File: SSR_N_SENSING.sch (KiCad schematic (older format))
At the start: 19 parts, among them J1 CONN_01X01, J2 CONN_01X01, J3 CONN_01X01, J4 CONN_01X01, Q1 BC850, U3 ACS722

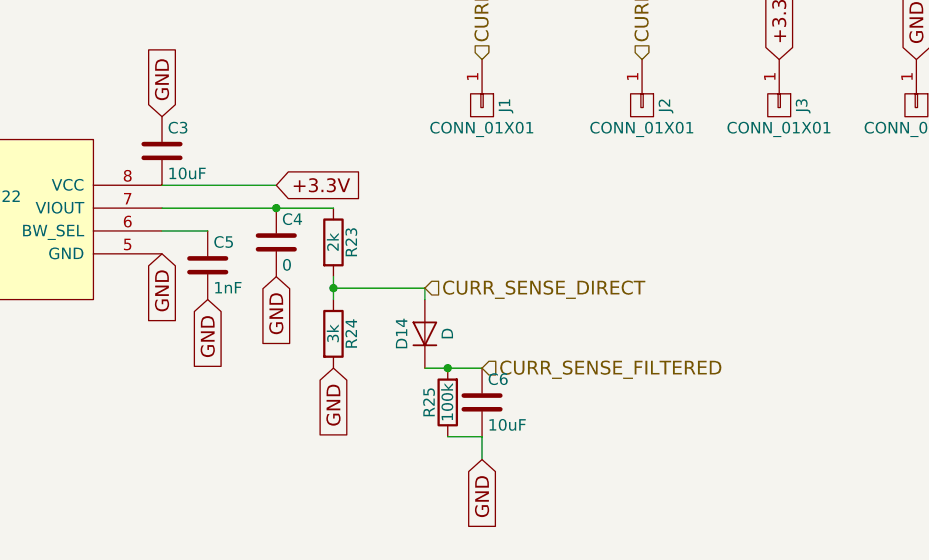
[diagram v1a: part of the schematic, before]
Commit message: I have redirected the output of the acs722 current sensing module directly to the ad converter. In theory this should increase the scale of the current sensing.
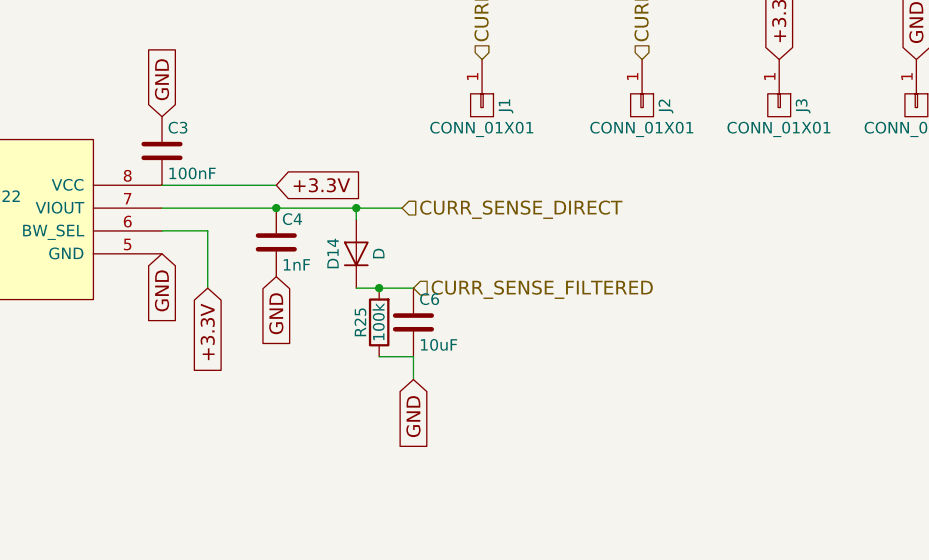
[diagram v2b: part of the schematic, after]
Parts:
- removed C5: 1nF, Capacitors_SMD:C_1206_HandSoldering, symbol C
- removed R23: 2k, Resistors_SMD:R_1206_HandSoldering, symbol R
- removed R24: 3k, Resistors_SMD:R_1206_HandSoldering, symbol R
- C3: value 10uF -> 100nF
- C4: value 0 -> 1nF; Comment This is NOT Necessary -> (none)
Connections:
- net +3.3V: now also U3.6 (BW_SEL)
- net CURR_SENSE_DIRECT: now also C4.1, U3.7 (VIOUT)
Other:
- moved on the sheet: C6, D14, R25
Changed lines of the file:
@@
 P 4950 4100
 F 0 "C3" H 4975 4200 50  0000 L CNN
-F 1 "10uF" H 4975 4000 50  0000 L CNN
+F 1 "100nF" H 4975 4000 50  0000 L CNN
 F 2 "Capacitors_SMD:C_1206_HandSoldering" H 4988 3950 30  0001 C CNN
-F 3 "http://hu.farnell.com/vishay/vj1206y106kxxtw1bc/cap-mlcc-x7r-10uf-25v-1206/dp/2407348" H 4950 4100 60  0001 C CNN
+F 3 "" H 4950 4100 60  0001 C CNN
 	1    4950 4100
 	1    0    0    -1
@@
 P 5450 4500
 F 0 "C4" H 5475 4600 50  0000 L CNN
-F 1 "0" H 5475 4400 50  0000 L CNN
+F 1 "1nF" H 5475 4400 50  0000 L CNN
 F 2 "Capacitors_SMD:C_1206_HandSoldering" H 5488 4350 30  0001 C CNN
 F 3 "" H 5450 4500 60  0000 C CNN
-F 4 "This is NOT Necessary" H 5450 4500 60  0001 C CNN "Comment"
 	1    5450 4500
 	1    0    0    -1
@@
 L D D14
 U 1 1 56251898
-P 6100 4900
-F 0 "D14" H 6100 5000 50  0000 C CNN
-F 1 "D" H 6100 4800 50  0000 C CNN
-F 2 "Diodes_SMD:D_SOD-123" H 6100 4900 60  0001 C CNN
-F 3 "http://hu.farnell.com/taiwan-semiconductor/b0540w/diode-rectif-40v-0-5a-sod123/dp/1863143" H 6100 4900 60  0001 C CNN
-	1    6100 4900
+P 5800 4550
+F 0 "D14" H 5800 4650 50  0000 C CNN
+F 1 "D" H 5800 4450 50  0000 C CNN
+F 2 "Diodes_SMD:D_SOD-123" H 5800 4550 60  0001 C CNN
+F 3 "http://hu.farnell.com/taiwan-semiconductor/b0540w/diode-rectif-40v-0-5a-sod123/dp/1863143" H 5800 4550 60  0001 C CNN
+	1    5800 4550
 	0    -1   -1   0
 $EndComp
@@
 L R R25
 U 1 1 5625189E
-P 6200 5200
-F 0 "R25" V 6280 5200 50  0000 C CNN
-F 1 "100k" V 6200 5200 50  0000 C CNN
-F 2 "Resistors_SMD:R_1206_HandSoldering" V 6130 5200 30  0001 C CNN
-F 3 "http://hu.farnell.com/vishay/crcw1206100kfkea/res-thick-film-100k-1-0-25w-1206/dp/1469975" H 6200 5200 30  0001 C CNN
-	1    6200 5200
+P 5900 4850
+F 0 "R25" V 5980 4850 50  0000 C CNN
+F 1 "100k" V 5900 4850 50  0000 C CNN
+F 2 "Resistors_SMD:R_1206_HandSoldering" V 5830 4850 30  0001 C CNN
+F 3 "http://hu.farnell.com/vishay/crcw1206100kfkea/res-thick-film-100k-1-0-25w-1206/dp/1469975" H 5900 4850 30  0001 C CNN
+	1    5900 4850
 	-1   0    0    1
 $EndComp
@@
 L C C6
 U 1 1 562518A4
-P 6350 5200
-F 0 "C6" H 6375 5300 50  0000 L CNN
-F 1 "10uF" H 6375 5100 50  0000 L CNN
-F 2 "Capacitors_SMD:C_1206_HandSoldering" H 6388 5050 30  0001 C CNN
-F 3 "" H 6350 5200 60  0000 C CNN
-	1    6350 5200
+P 6050 4850
+F 0 "C6" H 6075 4950 50  0000 L CNN
+F 1 "10uF" H 6075 4750 50  0000 L CNN
+F 2 "Capacitors_SMD:C_1206_HandSoldering" H 6088 4700 30  0001 C CNN
+F 3 "" H 6050 4850 60  0000 C CNN
+	1    6050 4850
 	1    0    0    -1
 $EndComp
-Text HLabel 6350 5050 2    60   Input ~ 0
+Text HLabel 6050 4700 2    60   Input ~ 0
 CURR_SENSE_FILTERED
-$Comp
-L C C5
-U 1 1 56251AFD
-P 5150 4600
-F 0 "C5" H 5175 4700 50  0000 L CNN
-F 1 "1nF" H 5175 4500 50  0000 L CNN
-F 2 "Capacitors_SMD:C_1206_HandSoldering" H 5188 4450 30  0001 C CNN
-F 3 "http://hu.farnell.com/vishay/vj1206y102kxeac/cap-mlcc-x7r-1000pf-500v-1206/dp/2407307" H 5150 4600 60  0001 C CNN
-	1    5150 4600
-	1    0    0    -1
-$EndComp
-Text HLabel 6100 4700 2    60   Input ~ 0
+Text HLabel 6000 4350 2    60   Input ~ 0
 CURR_SENSE_DIRECT
-$Comp
-L R R23
-U 1 1 56255AB8
-P 5700 4500
-F 0 "R23" V 5780 4500 50  0000 C CNN
-F 1 "2k" V 5700 4500 50  0000 C CNN
-F 2 "Resistors_SMD:R_1206_HandSoldering" V 5630 4500 30  0001 C CNN
-F 3 "" H 5700 4500 30  0000 C CNN
-	1    5700 4500
-	1    0    0    -1
-$EndComp
-$Comp
-L R R24
-U 1 1 56255B3D
-P 5700 4900
-F 0 "R24" V 5780 4900 50  0000 C CNN
-F 1 "3k" V 5700 4900 50  0000 C CNN
-F 2 "Resistors_SMD:R_1206_HandSoldering" V 5630 4900 30  0001 C CNN
-F 3 "http://hu.farnell.com/vishay/crcw12063k00fkea/res-thick-film-3k-1-0-25w-1206/dp/1653121" H 5700 4900 30  0001 C CNN
-	1    5700 4900
-	1    0    0    -1
-$EndComp
 Wire Wire Line
 	3450 2200 3550 2200
@@
 Connection ~ 3450 4250
 Wire Wire Line
-	6100 5050 6350 5050
-Connection ~ 6200 5050
+	5800 4700 6050 4700
+Connection ~ 5900 4700
 Wire Wire Line
-	6200 5350 6350 5350
+	5900 5000 6050 5000
 Wire Wire Line
-	6350 5350 6350 5450
+	6050 5000 6050 5100
 Wire Wire Line
 	4950 4450 5150 4450
 Wire Wire Line
-	4950 4350 5700 4350
+	4950 4350 6000 4350
 Connection ~ 5450 4350
 Wire Wire Line
-	5700 4650 5700 4750
-Wire Wire Line
-	5700 4700 6100 4700
-Connection ~ 5700 4700
-Wire Wire Line
-	6100 4700 6100 4750
+	5800 4350 5800 4400
 Connection ~ 3650 2000
 Wire Wire Line
@@
 Text GLabel 5450 4250 2    60   Input ~ 0
 +3.3V
-Text GLabel 5150 4750 3    60   Input ~ 0
-GND
-Text GLabel 5700 5050 3    60   Input ~ 0
-GND
-Text GLabel 6350 5450 3    60   Input ~ 0
+Text GLabel 6050 5100 3    60   Input ~ 0
 GND
 Text GLabel 4950 3950 1    60   Input ~ 0
@@
 Text GLabel 8250 3700 1    60   Input ~ 0
 GND
+Text GLabel 5150 4700 3    60   Input ~ 0
++3.3V
+Wire Wire Line
+	5150 4450 5150 4700
+Connection ~ 5800 4350
 $EndSCHEMATC

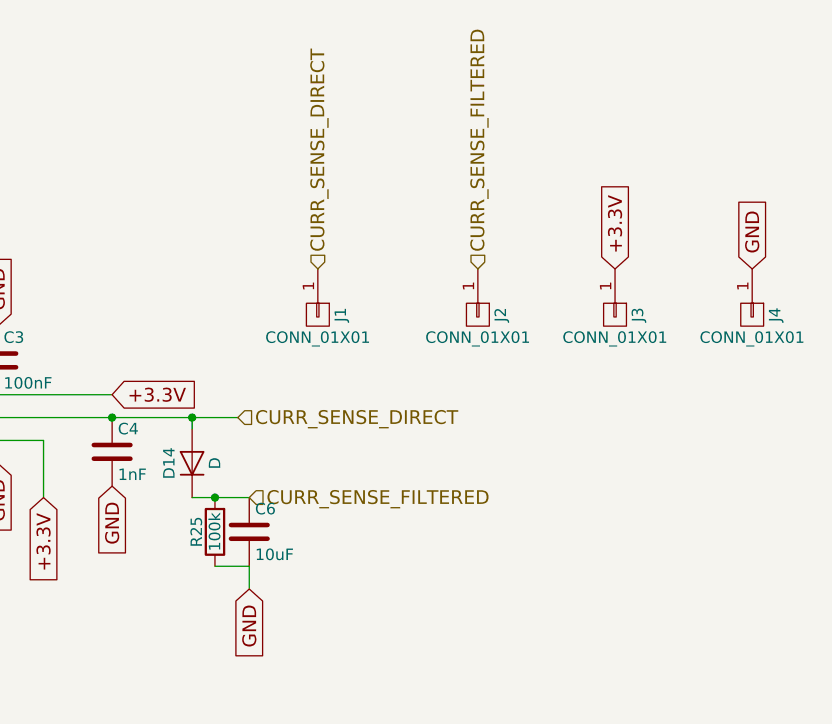
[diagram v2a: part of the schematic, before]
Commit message: this version contains the datasheets and the footprints of the parts
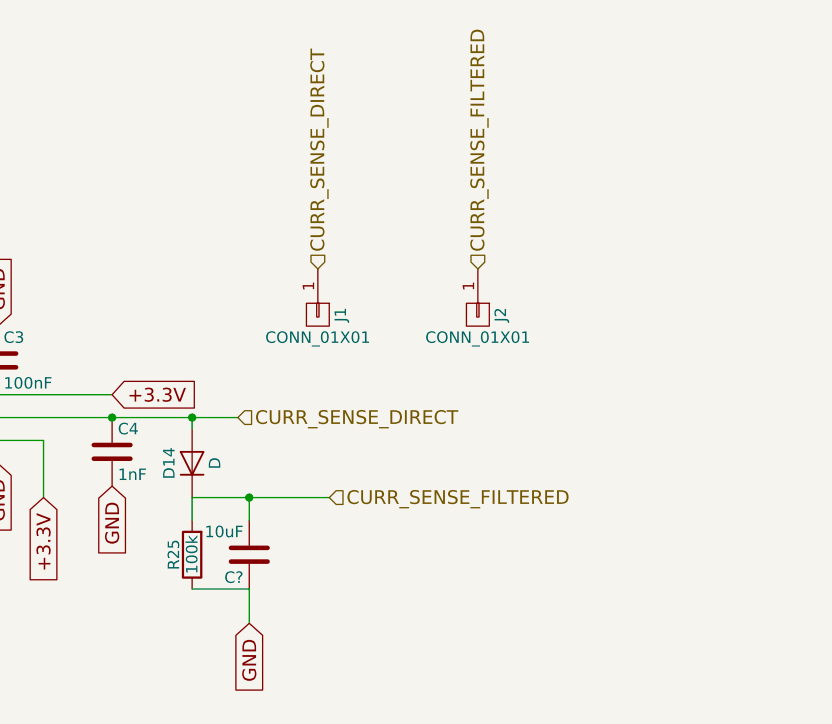
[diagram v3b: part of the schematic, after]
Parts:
- removed C6: 10uF, Capacitors_SMD:C_1206_HandSoldering, symbol C
- removed J3, J4: CONN_01X01, Connectors:PINTST, symbol CONN_01X01
- added C?: 10uF, Capacitors_SMD:C_0603_HandSoldering, symbol C
- C3, C4: footprint Capacitors_SMD:C_1206_HandSoldering -> Capacitors_SMD:C_0603_HandSoldering
- Q1: alt (none) -> http://hu.farnell.com/on-semiconductor/bc850clt1g/transisto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
- R21, R22, R25: footprint Resistors_SMD:R_1206_HandSoldering -> Resistors_SMD:R_0603_HandSoldering
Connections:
- net CURR_SENSE_FILTERED: now also C?.2
- net GND: now also C?.1
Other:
- moved on the sheet: R25
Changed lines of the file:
@@
 F 0 "R22" V 3880 2300 50  0000 C CNN
 F 1 "150" V 3800 2300 50  0000 C CNN
-F 2 "Resistors_SMD:R_1206_HandSoldering" V 3730 2300 30  0001 C CNN
-F 3 "hu.farnell.com/multicomp/mcwr12x1500ftl/res-thick-film-150-ohm-1-0-25w/dp/2447466" H 3800 2300 30  0001 C CNN
+F 2 "Resistors_SMD:R_0603_HandSoldering" V 3730 2300 30  0001 C CNN
+F 3 "hu.farnell.com/multicomp/mcwr06x1500ftl/res-thick-film-150-ohm-1-0-1w/dp/2447255" H 3800 2300 30  0001 C CNN
 	1    3800 2300
 	0    1    1    0
@@
 F 0 "R21" V 4230 1800 50  0000 C CNN
 F 1 "1k" V 4150 1800 50  0000 C CNN
-F 2 "Resistors_SMD:R_1206_HandSoldering" V 4080 1800 30  0001 C CNN
-F 3 "http://hu.farnell.com/multicomp/mcwr12x1001ftl/res-thick-film-1k-1-0-25w-1206/dp/2447473" H 4150 1800 30  0001 C CNN
+F 2 "Resistors_SMD:R_0603_HandSoldering" V 4080 1800 30  0001 C CNN
+F 3 "hu.farnell.com/multicomp/mcmr06x1001ftl/res-ceramic-1k-1-0-1w-0603/dp/2073348" H 4150 1800 30  0001 C CNN
 	1    4150 1800
 	0    1    1    0
@@
 F 1 "BC850" H 4000 1800 50  0000 L CNN
 F 2 "Housings_SOT-23_SOT-143_TSOT-6:SOT-23" H 4000 1725 50  0001 L CIN
-F 3 "" H 3800 1800 50  0001 L CNN
+F 3 "http://hu.farnell.com/nxp/bc850bw/trans-npn-45v-100mhz-sot-323-3/dp/2575203" H 3800 1800 50  0001 L CNN
+F 4 "http://hu.farnell.com/on-semiconductor/bc850clt1g/transistor-npn-45v-0-1a-sot-23/dp/2101810" H 3800 1800 60  0001 C CNN "alt"
 	1    3800 1800
 	-1   0    0    1
@@
 F 0 "C3" H 4975 4200 50  0000 L CNN
 F 1 "100nF" H 4975 4000 50  0000 L CNN
-F 2 "Capacitors_SMD:C_1206_HandSoldering" H 4988 3950 30  0001 C CNN
-F 3 "" H 4950 4100 60  0001 C CNN
+F 2 "Capacitors_SMD:C_0603_HandSoldering" H 4988 3950 30  0001 C CNN
+F 3 "hu.farnell.com/avx/06035c104kat2a/cap-mlcc-x7r-100nf-50v-0603/dp/1301804" H 4950 4100 60  0001 C CNN
 	1    4950 4100
 	1    0    0    -1
@@
 F 0 "C4" H 5475 4600 50  0000 L CNN
 F 1 "1nF" H 5475 4400 50  0000 L CNN
-F 2 "Capacitors_SMD:C_1206_HandSoldering" H 5488 4350 30  0001 C CNN
-F 3 "" H 5450 4500 60  0000 C CNN
+F 2 "Capacitors_SMD:C_0603_HandSoldering" H 5488 4350 30  0001 C CNN
+F 3 "hu.farnell.com/avx/06035a102jat2a/cap-mlcc-c0g-np0-1nf-50v-0603/dp/317202" H 5450 4500 60  0001 C CNN
 	1    5450 4500
 	1    0    0    -1
@@
 L R R25
 U 1 1 5625189E
-P 5900 4850
-F 0 "R25" V 5980 4850 50  0000 C CNN
-F 1 "100k" V 5900 4850 50  0000 C CNN
-F 2 "Resistors_SMD:R_1206_HandSoldering" V 5830 4850 30  0001 C CNN
-F 3 "http://hu.farnell.com/vishay/crcw1206100kfkea/res-thick-film-100k-1-0-25w-1206/dp/1469975" H 5900 4850 30  0001 C CNN
-	1    5900 4850
+P 5800 4950
+F 0 "R25" V 5880 4950 50  0000 C CNN
+F 1 "100k" V 5800 4950 50  0000 C CNN
+F 2 "Resistors_SMD:R_0603_HandSoldering" V 5730 4950 30  0001 C CNN
+F 3 "hu.farnell.com/multicomp/mcmr06x104-jtl/res-ceramic-100k-5-0-1w-0603/dp/2073357" H 5800 4950 30  0001 C CNN
+	1    5800 4950
 	-1   0    0    1
 $EndComp
-$Comp
-L C C6
-U 1 1 562518A4
-P 6050 4850
-F 0 "C6" H 6075 4950 50  0000 L CNN
-F 1 "10uF" H 6075 4750 50  0000 L CNN
-F 2 "Capacitors_SMD:C_1206_HandSoldering" H 6088 4700 30  0001 C CNN
-F 3 "" H 6050 4850 60  0000 C CNN
-	1    6050 4850
-	1    0    0    -1
-$EndComp
-Text HLabel 6050 4700 2    60   Input ~ 0
+Text HLabel 6400 4700 2    60   Input ~ 0
 CURR_SENSE_FILTERED
 Text HLabel 6000 4350 2    60   Input ~ 0
@@
 Connection ~ 3450 4250
 Wire Wire Line
-	5800 4700 6050 4700
-Connection ~ 5900 4700
-Wire Wire Line
-	5900 5000 6050 5000
-Wire Wire Line
-	6050 5000 6050 5100
+	5800 4700 6400 4700
+Wire Wire Line
+	6050 5100 6050 5250
 Wire Wire Line
 	4950 4450 5150 4450
@@
 Text GLabel 5450 4250 2    60   Input ~ 0
 +3.3V
-Text GLabel 6050 5100 3    60   Input ~ 0
+Text GLabel 6050 5250 3    60   Input ~ 0
 GND
 Text GLabel 4950 3950 1    60   Input ~ 0
@@
 Text HLabel 7050 3700 1    60   Input ~ 0
 CURR_SENSE_FILTERED
-$Comp
-L CONN_01X01 J3
-U 1 1 59407658
-P 7650 3900
-F 0 "J3" H 7650 4000 50  0000 C CNN
-F 1 "CONN_01X01" V 7750 3900 50  0000 C CNN
-F 2 "Connectors:PINTST" H 7650 3900 50  0001 C CNN
-F 3 "" H 7650 3900 50  0001 C CNN
-	1    7650 3900
-	0    1    1    0
-$EndComp
-Text GLabel 7650 3700 1    60   Input ~ 0
-+3.3V
 Connection ~ 3450 4550
-$Comp
-L CONN_01X01 J4
-U 1 1 594039D5
-P 8250 3900
-F 0 "J4" H 8250 4000 50  0000 C CNN
-F 1 "CONN_01X01" V 8350 3900 50  0000 C CNN
-F 2 "Connectors:PINTST" H 8250 3900 50  0001 C CNN
-F 3 "" H 8250 3900 50  0001 C CNN
-	1    8250 3900
-	0    1    1    0
-$EndComp
-Text GLabel 8250 3700 1    60   Input ~ 0
-GND
 Text GLabel 5150 4700 3    60   Input ~ 0
 +3.3V
@@
 	5150 4450 5150 4700
 Connection ~ 5800 4350
+$Comp
+L C C?
+U 1 1 59A85C33
+P 6050 4950
+F 0 "C?" H 6075 5050 50  0000 L CNN
+F 1 "10uF" H 6075 4850 50  0000 L CNN
+F 2 "Capacitors_SMD:C_0603_HandSoldering" H 6088 4800 30  0001 C CNN
+F 3 "http://hu.farnell.com/murata/grm188r60g106me47d/cap-mlcc-x5r-10uf-4v-0603/dp/2688517" H 6050 4950 60  0001 C CNN
+F 4 "http://hu.farnell.com/avx/06036d106mat2a/cap-mlcc-x5r-10uf-6-3v-0603/dp/1833804" H 6050 4950 60  0001 C CNN "avx"
+	1    6050 4950
+	-1   0    0    1
+$EndComp
+Wire Wire Line
+	5800 4700 5800 4800
+Wire Wire Line
+	6050 4700 6050 4800
+Connection ~ 6050 4700
+Wire Wire Line
+	5800 5100 6050 5100
 $EndSCHEMATC
